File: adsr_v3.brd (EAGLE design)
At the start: 99.4 x 29.2 mm, 48 parts, among them IC1 LM324D, IC2 4052D, IC3 40106D, SW1_TIME TL2285 L, SW2_TRIG TL2285 L, T1 BC847

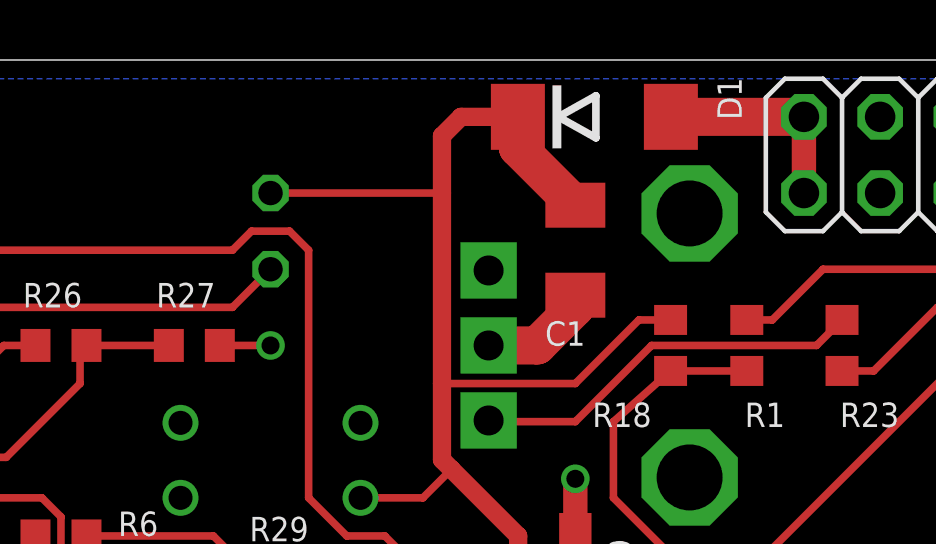
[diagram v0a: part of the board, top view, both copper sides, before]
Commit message: Moved PSU capacitor a bit.
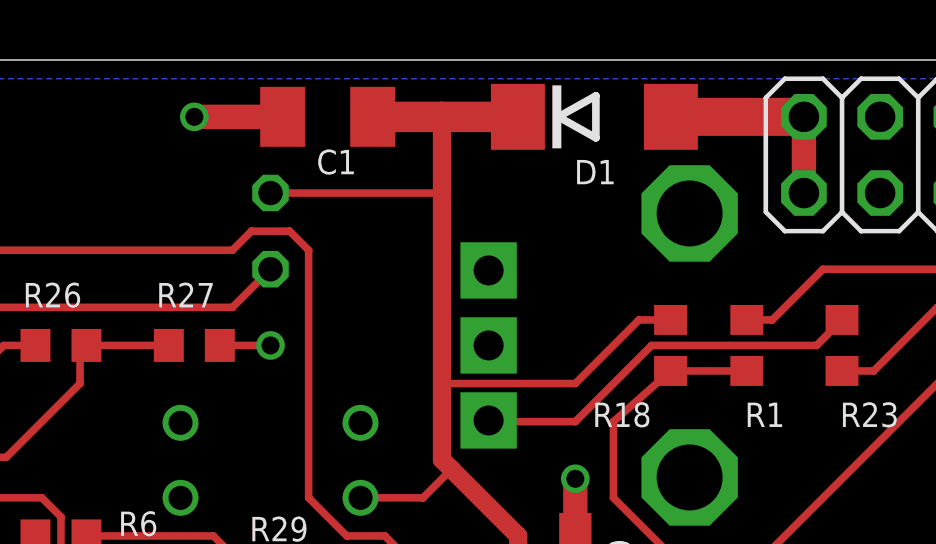
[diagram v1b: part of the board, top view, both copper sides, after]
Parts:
- moved C1 9.38 mm to (28.6, 38.1), turned to 180 degrees
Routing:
- net +12V: track 148.6 -> 147.5 mm
- net GND: track 55.9 -> 55.0 mm, vias 9 -> 10
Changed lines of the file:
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@@
 </autorouter>
 <elements>
-<element name="C1" library="rcl" package="C1206K" value="10u 16V" x="36.83" y="33.655" smashed="yes" rot="R270">
-<attribute name="NAME" x="37.16" y="31.285" size="0.8128" layer="25" font="vector" rot="R180"/>
+<element name="C1" library="rcl" package="C1206K" value="10u 16V" x="28.575" y="38.1" smashed="yes" rot="R180">
+<attribute name="NAME" x="29.54" y="37" size="0.8128" layer="25" font="vector" rot="R180"/>
 </element>
 <element name="C11" library="rcl" package="C1206K" value="4u7" x="60.96" y="17.78" smashed="yes" rot="R270">
@@
 </element>
 <element name="D1" library="diode" package="DO214AA" value="1N4004 equiv" x="37.465" y="38.1" smashed="yes">
-<attribute name="NAME" x="42.379" y="38" size="0.8128" layer="25" font="vector" ratio="10" rot="R90"/>
+<attribute name="NAME" x="38.2" y="36.664" size="0.8128" layer="25" font="vector" ratio="10" rot="R180"/>
 </element>
 <element name="D4" library="adafruit" package="SOD-323F" value="1N4148" x="88.9" y="17.145" smashed="yes" rot="R270">
@@
 <contactref element="C3" pad="2"/>
 <contactref element="R30" pad="1"/>
-<wire x1="36.83" y1="32.155" x2="36.83" y2="31.75" width="1.27" layer="1"/>
-<wire x1="36.83" y1="31.75" x2="35.56" y2="30.48" width="1.27" layer="1"/>
-<wire x1="35.56" y1="30.48" x2="33.94" y2="30.48" width="1.27" layer="1"/>
 <via x="30.48" y="18.415" extent="1-16" drill="0.6" shape="square"/>
 <wire x1="27.545" y1="20.32" x2="29.63" y2="20.32" width="0.254" layer="1"/>
@@
 <wire x1="76.9366" y1="15.875" x2="76.9366" y2="14.605" width="0.254" layer="1"/>
 <wire x1="24.98" y1="30.48" x2="26.67" y2="30.48" width="0.254" layer="1"/>
+<via x="24.13" y="38.1" extent="1-16" drill="0.6" shape="square"/>
+<wire x1="27.075" y1="38.1" x2="24.13" y2="38.1" width="0.8128" layer="1"/>
 </signal>
 <signal name="+12V">
@@
 <contactref element="SW_MANUAL" pad="5"/>
 <wire x1="32.385" y1="29.21" x2="32.385" y2="35.56" width="0.6096" layer="1"/>
-<wire x1="32.385" y1="35.56" x2="32.385" y2="37.465" width="0.6096" layer="1"/>
+<wire x1="32.385" y1="35.56" x2="32.385" y2="38.1" width="0.6096" layer="1"/>
 <wire x1="26.67" y1="15.24" x2="29.845" y2="15.24" width="0.254" layer="1"/>
 <wire x1="29.845" y1="15.24" x2="32.385" y2="17.78" width="0.254" layer="1"/>
@@
 <wire x1="38.95" y1="31.33" x2="36.83" y2="29.21" width="0.254" layer="1"/>
 <wire x1="36.83" y1="29.21" x2="32.385" y2="29.21" width="0.254" layer="1"/>
-<wire x1="32.385" y1="37.465" x2="33.02" y2="38.1" width="0.6096" layer="1"/>
-<wire x1="33.02" y1="38.1" x2="34.915" y2="38.1" width="0.6096" layer="1"/>
-<wire x1="34.915" y1="38.1" x2="34.915" y2="37.07" width="1.27" layer="1"/>
-<wire x1="34.915" y1="37.07" x2="36.83" y2="35.155" width="1.27" layer="1"/>
 <wire x1="87.28" y1="30.48" x2="85.09" y2="30.48" width="0.254" layer="1"/>
 <wire x1="85.09" y1="30.48" x2="80.405" y2="25.795" width="0.254" layer="1"/>
@@
 <wire x1="80.645" y1="19.05" x2="80.645" y2="21.59" width="0.254" layer="1"/>
 <wire x1="80.645" y1="21.59" x2="81.28" y2="22.225" width="0.254" layer="1"/>
+<wire x1="34.915" y1="38.1" x2="32.385" y2="38.1" width="1.016" layer="1"/>
+<wire x1="32.385" y1="38.1" x2="30.075" y2="38.1" width="1.016" layer="1"/>
 </signal>
 <signal name="SUST_LEVEL">

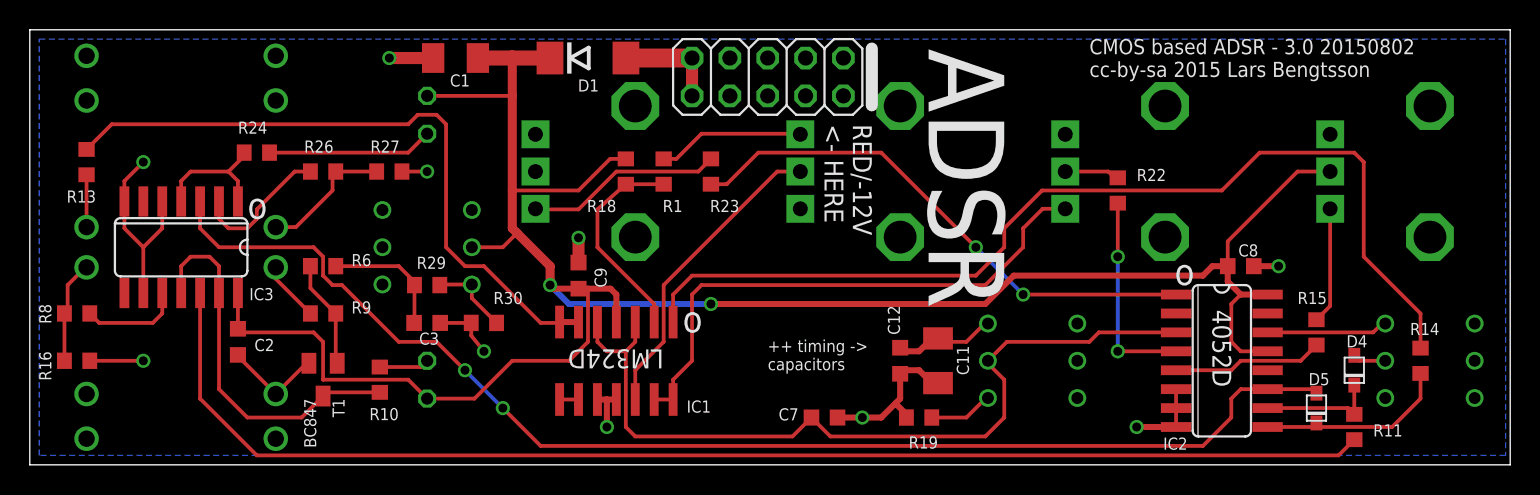
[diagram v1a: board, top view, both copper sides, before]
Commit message: Minor routing & labeling fixes. Replaced schematic A3 document frame with other type.
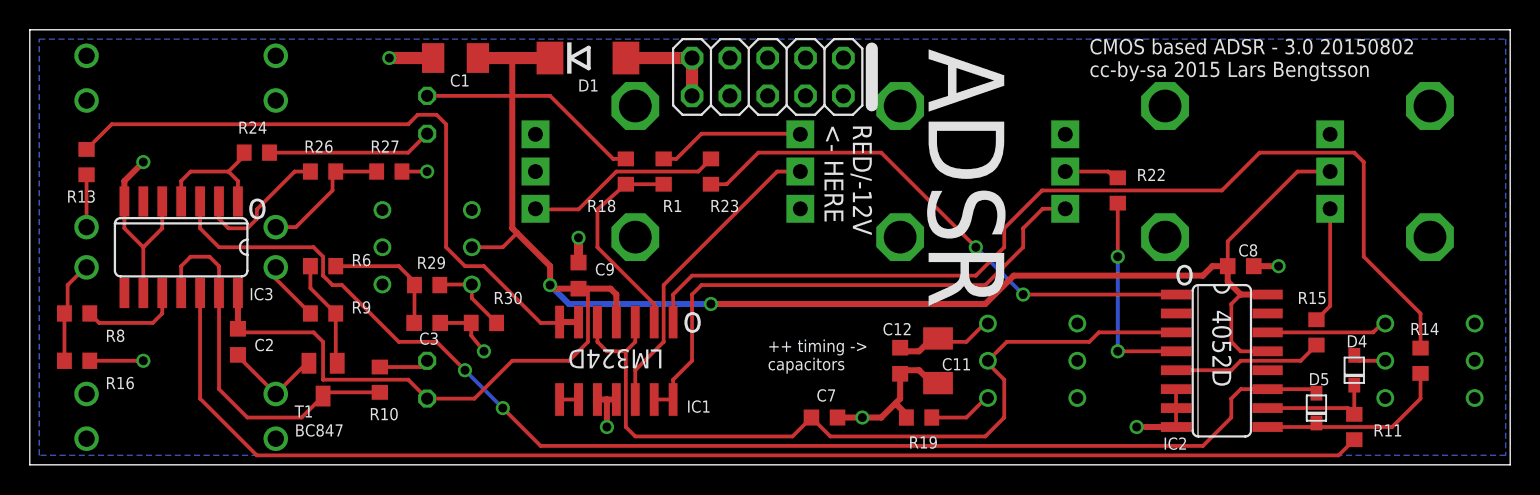
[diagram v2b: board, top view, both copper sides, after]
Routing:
- net +12V: track 147.5 -> 148.4 mm
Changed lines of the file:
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@@
 </element>
 <element name="C11" library="rcl" package="C1206K" value="4u7" x="60.96" y="17.78" smashed="yes" rot="R270">
-<attribute name="NAME" x="63.035" y="16.815" size="0.8128" layer="25" font="vector" rot="R90"/>
+<attribute name="NAME" x="63.195" y="17.95" size="0.8128" layer="25" font="vector" rot="R180"/>
 </element>
 <element name="C12" library="rcl" package="C0603K" value="4u7" x="58.42" y="17.78" smashed="yes" rot="R270">
-<attribute name="NAME" x="58.405" y="19.52" size="0.8128" layer="25" font="vector" rot="R90"/>
+<attribute name="NAME" x="59.22" y="20.305" size="0.8128" layer="25" font="vector" rot="R180"/>
 </element>
 <element name="C7" library="rcl" package="C0603K" value="470n" x="53.34" y="13.97" smashed="yes">
-<attribute name="NAME" x="51.6" y="14.59" size="0.8128" layer="25" font="vector" rot="R180"/>
+<attribute name="NAME" x="54.14" y="15.86" size="0.8128" layer="25" font="vector" rot="R180"/>
 </element>
 <element name="C8" library="rcl" package="C0603K" value="100n" x="81.28" y="24.13" smashed="yes">
@@
 </element>
 <element name="C9" library="rcl" package="C0603K" value="100n" x="36.83" y="23.495" smashed="yes" rot="R90">
-<attribute name="NAME" x="38.72" y="22.695" size="0.8128" layer="25" font="vector" rot="R90"/>
+<attribute name="NAME" x="37.935" y="23.51" size="0.8128" layer="25" font="vector"/>
 </element>
 <element name="D1" library="diode" package="DO214AA" value="1N4004 equiv" x="37.465" y="38.1" smashed="yes">
@@
 </element>
 <element name="PEAK_OUT" library="thonkiconn" package="WQP-PJ301M-12_JACK" value="WQP-PJ301M-12_JACK" x="16.51" y="31.75" smashed="yes" rot="MR180">
-<attribute name="NAME" x="12.0396" y="37.7952" size="1.27" layer="22" rot="MR180"/>
+<attribute name="NAME" x="21.2598" y="26.0096" size="1.27" layer="22" rot="MR90"/>
 </element>
 <element name="CV_OUT" library="thonkiconn" package="WQP-PJ301M-12_JACK" value="WQP-PJ301M-12_JACK" x="3.81" y="31.75" smashed="yes" rot="MR180">
-<attribute name="NAME" x="0.6096" y="37.7952" size="1.27" layer="22" rot="MR180"/>
+<attribute name="NAME" x="8.5598" y="26.0096" size="1.27" layer="22" rot="MR90"/>
 </element>
 <element name="R1" library="rcl" package="R0603" value="1k" x="42.545" y="30.48" smashed="yes" rot="R90">
@@
 <element name="SW2_TRIG" library="lb_devs" package="TL2285_PCB" value="TL2285 L" x="93.98" y="17.78" rot="MR90"/>
 <element name="T1" library="transistor" package="SOT23" value="BC847" x="19.685" y="16.51" smashed="yes" rot="R180">
-<attribute name="NAME" x="20.32" y="15.24" size="0.8128" layer="25" rot="R270"/>
-<attribute name="VALUE" x="18.415" y="15.24" size="0.8128" layer="25" rot="R270"/>
+<attribute name="NAME" x="17.78" y="13.97" size="0.8128" layer="25"/>
+<attribute name="VALUE" x="17.78" y="12.7" size="0.8128" layer="25"/>
 </element>
 <element name="SW_MANUAL" library="lb_devs" package="TL2285_PCB" value="TL2285 Mom." x="26.67" y="25.4" rot="MR90"/>
@@
 </element>
 <element name="R8" library="rcl" package="R0603" value="4k7" x="3.175" y="20.955" smashed="yes" rot="R180">
-<attribute name="NAME" x="0.635" y="21.59" size="0.8128" layer="25" font="vector" rot="R270"/>
+<attribute name="NAME" x="5.08" y="19.05" size="0.8128" layer="25" font="vector"/>
 </element>
 <element name="R16" library="rcl" package="R0603" value="3k3" x="3.175" y="17.78" smashed="yes">
-<attribute name="NAME" x="0.635" y="18.415" size="0.8128" layer="25" font="vector" rot="R270"/>
+<attribute name="NAME" x="5.08" y="15.875" size="0.8128" layer="25" font="vector"/>
 </element>
 <element name="R24" library="rcl" package="R0603" value="10k" x="15.24" y="31.75" smashed="yes" rot="R180">
@@
 </element>
 <element name="LED1" library="led" package="LED5MM" value="PEAK_LED" x="26.67" y="34.29" smashed="yes" rot="MR270">
-<attribute name="NAME" x="23.114" y="36.195" size="1.27" layer="26" ratio="10" rot="MR270"/>
+<attribute name="NAME" x="31.369" y="36.83" size="1.27" layer="26" ratio="10" rot="MR270"/>
 </element>
 <element name="R26" library="rcl" package="R0603" value="4k7" x="19.685" y="30.48" smashed="yes">
@@
 <contactref element="D1" pad="A"/>
 <wire x1="44.45" y1="38.1" x2="44.45" y2="35.56" width="0.8128" layer="1"/>
-<wire x1="44.45" y1="38.1" x2="40.015" y2="38.1" width="1.27" layer="1"/>
+<wire x1="44.45" y1="38.1" x2="40.015" y2="38.1" width="0.8128" layer="1"/>
 </signal>
 <signal name="GND">
@@
 <via x="38.735" y="13.335" extent="1-16" drill="0.6" shape="square"/>
 <via x="36.83" y="26.035" extent="1-16" drill="0.6" shape="square"/>
-<wire x1="36.83" y1="24.37" x2="36.83" y2="26.035" width="0.8128" layer="1"/>
+<wire x1="36.83" y1="24.37" x2="36.83" y2="26.035" width="0.6096" layer="1"/>
 <contactref element="IC1" pad="10"/>
 <contactref element="R16" pad="2"/>
@@
 <wire x1="18.57" y1="17.61" x2="16.51" y2="15.55" width="0.254" layer="1"/>
 <via x="26.67" y="30.48" extent="1-16" drill="0.6" shape="square"/>
-<wire x1="7.62" y1="31.115" x2="6.35" y2="29.845" width="0.254" layer="1"/>
-<wire x1="6.35" y1="29.845" x2="6.35" y2="28.4734" width="0.254" layer="1"/>
+<wire x1="7.62" y1="31.115" x2="6.35" y2="29.845" width="0.4064" layer="1"/>
+<wire x1="6.35" y1="29.845" x2="6.35" y2="28.4734" width="0.4064" layer="1"/>
 <wire x1="8.89" y1="28.4734" x2="8.89" y2="26.67" width="0.254" layer="1"/>
 <wire x1="8.89" y1="26.67" x2="7.62" y2="25.4" width="0.254" layer="1"/>
@@
 <wire x1="36.195" y1="21.59" x2="45.72" y2="21.59" width="0.4064" layer="16"/>
 <via x="45.72" y="21.59" extent="1-16" drill="0.6" shape="square"/>
-<wire x1="34.925" y1="22.86" x2="34.925" y2="24.13" width="0.6096" layer="1"/>
+<wire x1="34.925" y1="22.86" x2="34.925" y2="24.13" width="0.4064" layer="1"/>
 <wire x1="36.83" y1="22.62" x2="35.165" y2="22.62" width="0.4064" layer="1"/>
 <wire x1="35.165" y1="22.62" x2="34.925" y2="22.86" width="0.4064" layer="1"/>
@@
 <wire x1="38.975" y1="22.62" x2="39.37" y2="22.225" width="0.4064" layer="1"/>
 <wire x1="39.37" y1="22.225" x2="39.37" y2="20.38" width="0.4064" layer="1"/>
-<wire x1="34.925" y1="24.13" x2="32.7025" y2="26.3525" width="0.6096" layer="1"/>
-<wire x1="32.7025" y1="26.3525" x2="32.385" y2="26.67" width="0.6096" layer="1"/>
-<wire x1="32.385" y1="26.67" x2="32.385" y2="29.21" width="0.6096" layer="1"/>
+<wire x1="34.925" y1="24.13" x2="32.7025" y2="26.3525" width="0.4064" layer="1"/>
+<wire x1="32.7025" y1="26.3525" x2="32.385" y2="26.67" width="0.4064" layer="1"/>
 <contactref element="SW_MANUAL" pad="5"/>
-<wire x1="32.385" y1="29.21" x2="32.385" y2="35.56" width="0.6096" layer="1"/>
-<wire x1="32.385" y1="35.56" x2="32.385" y2="38.1" width="0.6096" layer="1"/>
+<wire x1="32.385" y1="26.67" x2="32.385" y2="35.56" width="0.4064" layer="1"/>
+<wire x1="32.385" y1="35.56" x2="32.385" y2="38.1" width="0.4064" layer="1"/>
 <wire x1="26.67" y1="15.24" x2="29.845" y2="15.24" width="0.254" layer="1"/>
 <wire x1="29.845" y1="15.24" x2="32.385" y2="17.78" width="0.254" layer="1"/>
@@
 <wire x1="80.405" y1="24.13" x2="80.405" y2="25.795" width="0.254" layer="1"/>
 <contactref element="R5" pad="P$2"/>
-<wire x1="40.005" y1="31.33" x2="38.95" y2="31.33" width="0.254" layer="1"/>
-<wire x1="38.95" y1="31.33" x2="36.83" y2="29.21" width="0.254" layer="1"/>
-<wire x1="36.83" y1="29.21" x2="32.385" y2="29.21" width="0.254" layer="1"/>
 <wire x1="87.28" y1="30.48" x2="85.09" y2="30.48" width="0.254" layer="1"/>
 <wire x1="85.09" y1="30.48" x2="80.405" y2="25.795" width="0.254" layer="1"/>
 <contactref element="IC3" pad="14"/>
 <contactref element="C2" pad="1"/>
-<wire x1="13.97" y1="22.3266" x2="13.97" y2="19.925" width="0.254" layer="1"/>
+<wire x1="13.97" y1="22.3266" x2="13.97" y2="19.925" width="0.4064" layer="1"/>
 <wire x1="26.67" y1="15.24" x2="25.4" y2="16.51" width="0.254" layer="1"/>
 <wire x1="25.4" y1="16.51" x2="19.685" y2="16.51" width="0.254" layer="1"/>
@@
 <wire x1="80.645" y1="19.05" x2="80.645" y2="21.59" width="0.254" layer="1"/>
 <wire x1="80.645" y1="21.59" x2="81.28" y2="22.225" width="0.254" layer="1"/>
-<wire x1="34.915" y1="38.1" x2="32.385" y2="38.1" width="1.016" layer="1"/>
-<wire x1="32.385" y1="38.1" x2="30.075" y2="38.1" width="1.016" layer="1"/>
+<wire x1="34.915" y1="38.1" x2="32.385" y2="38.1" width="0.8128" layer="1"/>
+<wire x1="32.385" y1="38.1" x2="30.075" y2="38.1" width="0.8128" layer="1"/>
+<wire x1="40.005" y1="31.33" x2="39.155" y2="31.33" width="0.254" layer="1"/>
+<wire x1="39.155" y1="31.33" x2="34.925" y2="35.56" width="0.254" layer="1"/>
+<wire x1="34.925" y1="35.56" x2="32.385" y2="35.56" width="0.254" layer="1"/>
 </signal>
 <signal name="SUST_LEVEL">

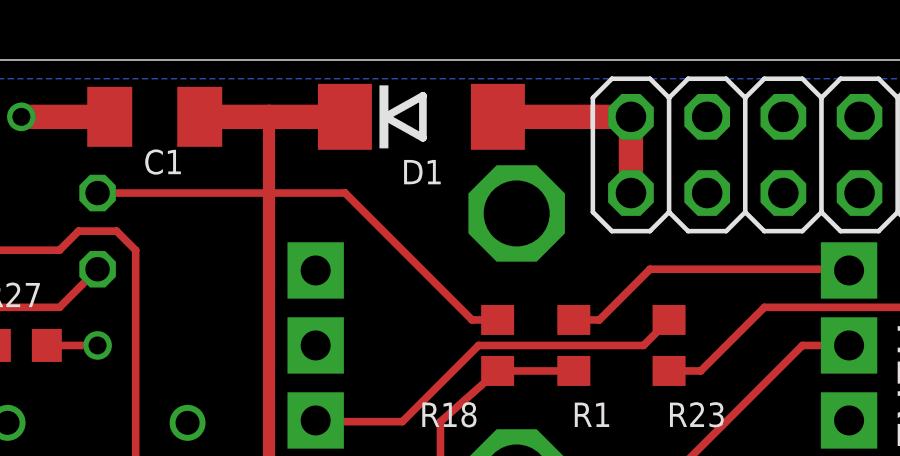
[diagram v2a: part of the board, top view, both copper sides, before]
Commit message: Moved PSU diode and capacitor a bit. Diode has a rather bit and wide package, we better leave a bit of space around it.
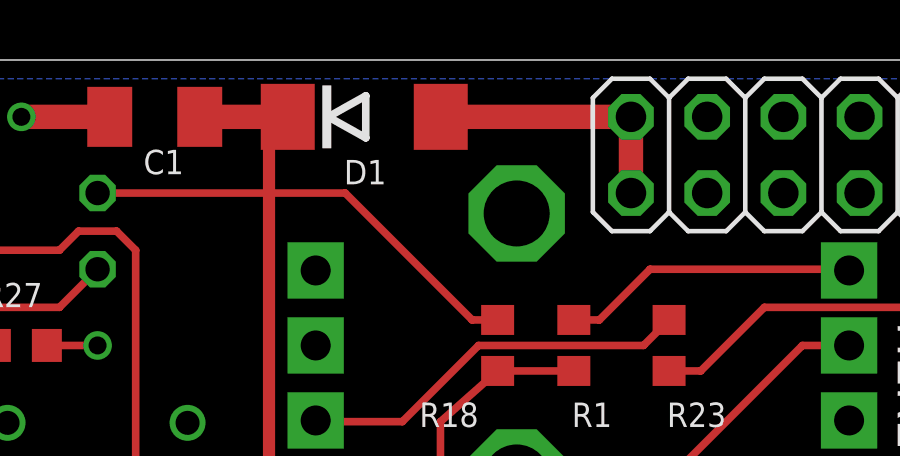
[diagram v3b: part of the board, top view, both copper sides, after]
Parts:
- moved D1 1.91 mm to (35.6, 38.1)
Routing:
- net N$3: track 6.98 -> 8.88 mm
- net +12V: track 148.4 -> 146.5 mm
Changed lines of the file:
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@@
 <attribute name="NAME" x="37.935" y="23.51" size="0.8128" layer="25" font="vector"/>
 </element>
-<element name="D1" library="diode" package="DO214AA" value="1N4004 equiv" x="37.465" y="38.1" smashed="yes">
-<attribute name="NAME" x="38.2" y="36.664" size="0.8128" layer="25" font="vector" ratio="10" rot="R180"/>
+<element name="D1" library="diode" package="DO214AA" value="1N4004 equiv" x="35.56" y="38.1" smashed="yes">
+<attribute name="NAME" x="36.295" y="36.664" size="0.8128" layer="25" font="vector" ratio="10" rot="R180"/>
 </element>
 <element name="D4" library="adafruit" package="SOD-323F" value="1N4148" x="88.9" y="17.145" smashed="yes" rot="R270">
@@
 <contactref element="D1" pad="A"/>
 <wire x1="44.45" y1="38.1" x2="44.45" y2="35.56" width="0.8128" layer="1"/>
-<wire x1="44.45" y1="38.1" x2="40.015" y2="38.1" width="0.8128" layer="1"/>
+<wire x1="44.45" y1="38.1" x2="38.11" y2="38.1" width="0.8128" layer="1"/>
 </signal>
 <signal name="GND">
@@
 <wire x1="80.645" y1="19.05" x2="80.645" y2="21.59" width="0.254" layer="1"/>
 <wire x1="80.645" y1="21.59" x2="81.28" y2="22.225" width="0.254" layer="1"/>
-<wire x1="34.915" y1="38.1" x2="32.385" y2="38.1" width="0.8128" layer="1"/>
+<wire x1="33.01" y1="38.1" x2="32.385" y2="38.1" width="0.8128" layer="1"/>
 <wire x1="32.385" y1="38.1" x2="30.075" y2="38.1" width="0.8128" layer="1"/>
 <wire x1="40.005" y1="31.33" x2="39.155" y2="31.33" width="0.254" layer="1"/>

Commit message: Changed LED current resistors to 27k, better match with the 350-400 mcd LEDs.
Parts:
- R10, R24: value 10k -> 27k
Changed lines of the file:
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@@
 <attribute name="NAME" x="43.815" y="28.575" size="0.8128" layer="25" font="vector" rot="R180"/>
 </element>
-<element name="R10" library="rcl" package="R0603" value="10k" x="23.495" y="16.51" smashed="yes" rot="R270">
+<element name="R10" library="rcl" package="R0603" value="27k" x="23.495" y="16.51" smashed="yes" rot="R270">
 <attribute name="NAME" x="24.765" y="14.605" size="0.8128" layer="25" font="vector" rot="R180"/>
 </element>
@@
 <attribute name="NAME" x="5.08" y="15.875" size="0.8128" layer="25" font="vector"/>
 </element>
-<element name="R24" library="rcl" package="R0603" value="10k" x="15.24" y="31.75" smashed="yes" rot="R180">
+<element name="R24" library="rcl" package="R0603" value="27k" x="15.24" y="31.75" smashed="yes" rot="R180">
 <attribute name="NAME" x="13.97" y="33.02" size="0.8128" layer="25" font="vector"/>
 </element>
